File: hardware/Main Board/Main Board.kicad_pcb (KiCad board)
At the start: 4 copper layers, 65 x 56 mm, 29 parts, among them J1 Motor Power, J2 DEC Motor, J3 RA Motor, J4 Conn_01x05_Female, P1 Conn_02x20_Odd_Even, Q1 2N3904, Q2 2N3904, Q3 2N3904, Q4 2N3904, Q5 2N3904, U1 ELEGOO, U2 ELEGOO

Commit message: First Routing...
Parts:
- added J5: Joystick Connector, Connector_JST:JST_PH_B5B-PH-K_1x05_P2.00mm_Vertical, F.Cu at (253.5, 110.8)
- added J6: System Debug, Connector_PinHeader_1.27mm:PinHeader_1x03_P1.27mm_Vertical, F.Cu at (199.8, 108.2)
- added J7: DEC Debug, Connector_PinHeader_1.27mm:PinHeader_1x05_P1.27mm_Vertical, F.Cu at (206.2, 132.2)
- added J8: RA Debug, Connector_PinHeader_1.27mm:PinHeader_1x05_P1.27mm_Vertical, F.Cu at (230.0, 132.5)
- J4: value Conn_01x05_Female -> Joystick Debug; footprint Connector_JST:JST_PH_B5B-PH-K_1x05_P2.00mm_Vertical -> Connector_PinHeader_1.27mm:PinHeader_1x03_P1.27mm_Vertical
- R2, R7: value 100K -> 22K
- R5, R6: value 22K -> 100K
- U1: value ELEGOO -> RA Driver
- moved R12 38.9 mm to (246.8, 148.5), turned to 90 degrees
- moved Q5 34.7 mm to (248.8, 140.5), turned to 270 degrees
- moved R8 27.8 mm to (258.5, 130.8), turned to 90 degrees
- moved J4 27.2 mm to (259.2, 108.2), turned to 0 degrees
- moved R7 22.9 mm to (258.0, 134.8), turned to 270 degrees
- moved R11 22.5 mm to (252.0, 148.5), turned to 90 degrees
- moved R9 20.7 mm to (251.0, 136.5), turned to 90 degrees
- moved R5 19.3 mm to (242.8, 123.5), turned to 0 degrees
- moved R3 18.0 mm to (258.8, 117.6), turned to 270 degrees
- moved R4 17.8 mm to (249.7, 123.5), turned to 180 degrees
- moved R10 14.9 mm to (247.5, 134.8), turned to 270 degrees
- moved R6 14.8 mm to (254.5, 136.5), turned to 90 degrees
- moved Q3 13.9 mm to (253.5, 130.8)
- moved Q4 13.4 mm to (246.2, 130.8), turned to 90 degrees
- moved J1 10.9 mm to (219.2, 144.5)
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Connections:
- J4 pad 3: +5V -> Net-(J4-Pad3)
- P1 pad 25: Net-(P1-Pad25) -> GND
- Q1 pad 3: /GPIO10(SPI0_MOSI) -> /ID_SD
- Q2 pad 3: /ID_SD -> /GPIO22(GEN3)
- Q3 pad 3: /GPIO9(SPI0_MISO) -> /GPIO11(SPI0_SCK)
- Q4 pad 3: /GPIO25(GEN6) -> /GPIO9(SPI0_MISO)
- Q5 pad 3: /GPIO11(SPI0_SCK) -> /GPIO10(SPI0_MOSI)
- R1 pad 1: Net-(Q1-Pad2) -> +3V3
- R1 pad 2: Net-(J4-Pad5) -> /ID_SD
- R10 pad 1: Net-(Q3-Pad2) -> Net-(Q4-Pad2)
- R10 pad 2: Net-(J4-Pad1) -> Net-(J4-Pad3)
- R11 pad 1: Net-(Q4-Pad2) -> Net-(Q5-Pad2)
- R11 pad 2: Net-(J4-Pad2) -> Net-(J4-Pad1)
- R12 pad 1: Net-(Q5-Pad2) -> +3V3
- R12 pad 2: Net-(J4-Pad1) -> /GPIO10(SPI0_MOSI)
- R2 pad 1: +3V3 -> Net-(Q1-Pad2)
- R2 pad 2: /GPIO10(SPI0_MOSI) -> GND
- R3 pad 2: /ID_SD -> /GPIO22(GEN3)
- R4 pad 1: +3V3 -> Net-(Q1-Pad2)
- R4 pad 2: /GPIO9(SPI0_MISO) -> Net-(J4-Pad2)
- R5 pad 2: GND -> Net-(J4-Pad2)
- R6 pad 1: Net-(Q3-Pad2) -> +3V3
- R6 pad 2: GND -> /GPIO11(SPI0_SCK)
- R7 pad 1: +3V3 -> Net-(Q3-Pad2)
- R7 pad 2: /GPIO25(GEN6) -> GND
- R8 pad 2: /GPIO11(SPI0_SCK) -> /GPIO9(SPI0_MISO)
- R9 pad 1: Net-(Q2-Pad2) -> Net-(Q3-Pad2)
- R9 pad 2: Net-(J4-Pad2) -> Net-(J4-Pad3)
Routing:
- net /GPIO22(GEN3): track 0.00 -> 48.7 mm
- net /GPIO25(GEN6): track 43.0 -> 0.00 mm, vias 1 -> 0
- net Net-(J4-Pad3): track 0.00 -> 37.4 mm
- net /GPIO2(SDA1): track 9.48 -> 44.2 mm
- net Net-(J4-Pad1): track 28.1 -> 56.3 mm
- net /GPIO5: track 7.36 -> 34.5 mm
- net +3V3: track 0.00 -> 24.4 mm
- net /GPIO6: track 11.2 -> 35.1 mm
- net /GPIO4(GCLK): track 21.7 -> 43.2 mm
- net /GPIO3(SCL1): track 13.1 -> 34.5 mm
- net /GPIO13(PWM1): track 14.7 -> 35.6 mm
- net Net-(J4-Pad5): track 19.3 -> 0.00 mm
- net /GPIO11(SPI0_SCK): track 27.5 -> 43.9 mm
- net /ID_SD: track 14.2 -> 28.4 mm
- net /GPIO17(GEN0): track 26.4 -> 40.2 mm
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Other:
- net class Motor Power added: clearance 0.2, trace_width 0.2, via_dia 0.9, via_drill 0.6
- board text removed: "RASPBERRY-PI 40-PIN ADDON BOARD VIEW FROM TOP NOTE: P1 SHOULD BE FITTED ON THE REVERSE OF THE BOARD ADD EDGE CUTS FROM CAMERA AND DISPLAY PORTS AS REQUIRED"
- board text removed: "RJ45"
- board text removed: "USB"

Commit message: Ready to Build the Board
release_1.0
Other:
- board text added: "+"
- board text added: "-"
- board text added: "DBG"
- board text added: "DEC Motor"
- board text added: "Joystick"
- board text added: "Motor Power"
- board text added: "RA Motor"
- board text added: "https://github.com/eruditelite/pimount.git"
- board text added: "release_1.0"

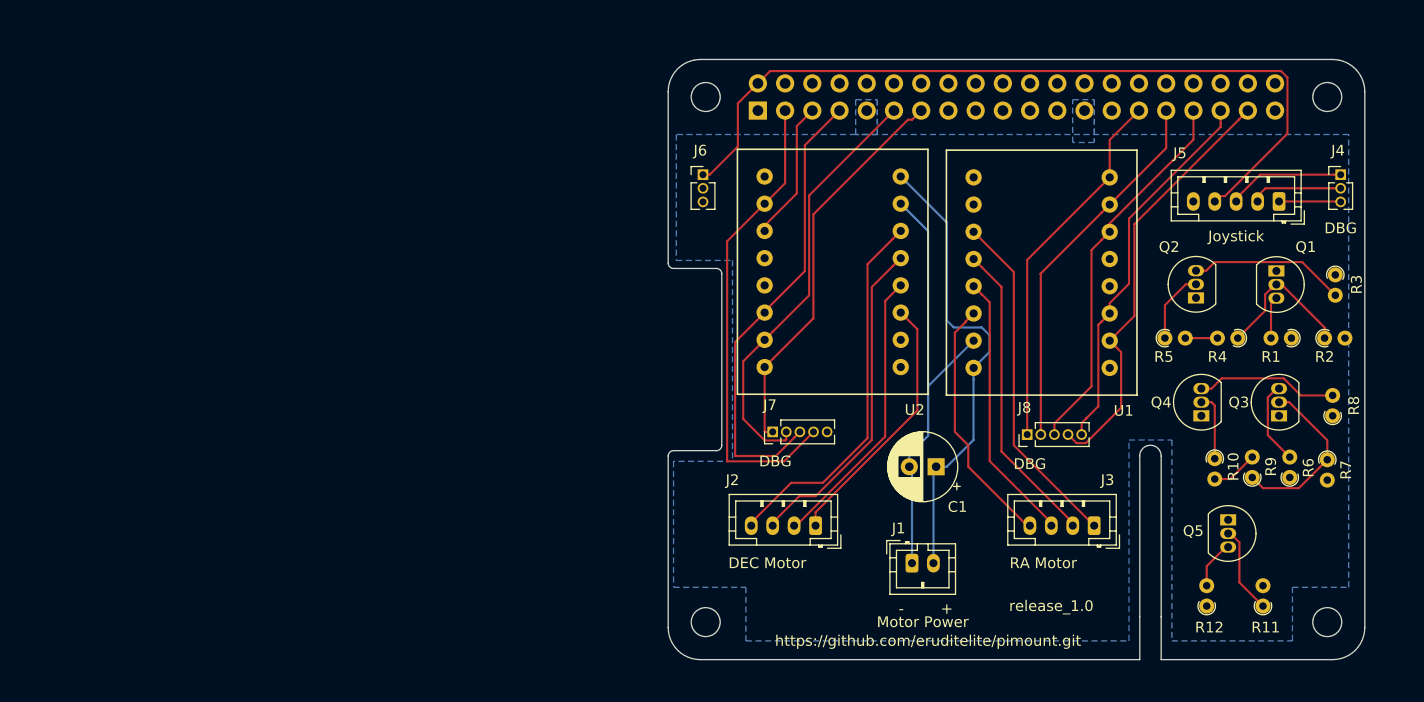
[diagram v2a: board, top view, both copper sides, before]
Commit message: Extended the Size of the Board
Include space for the DC to DC converters and
re-route.
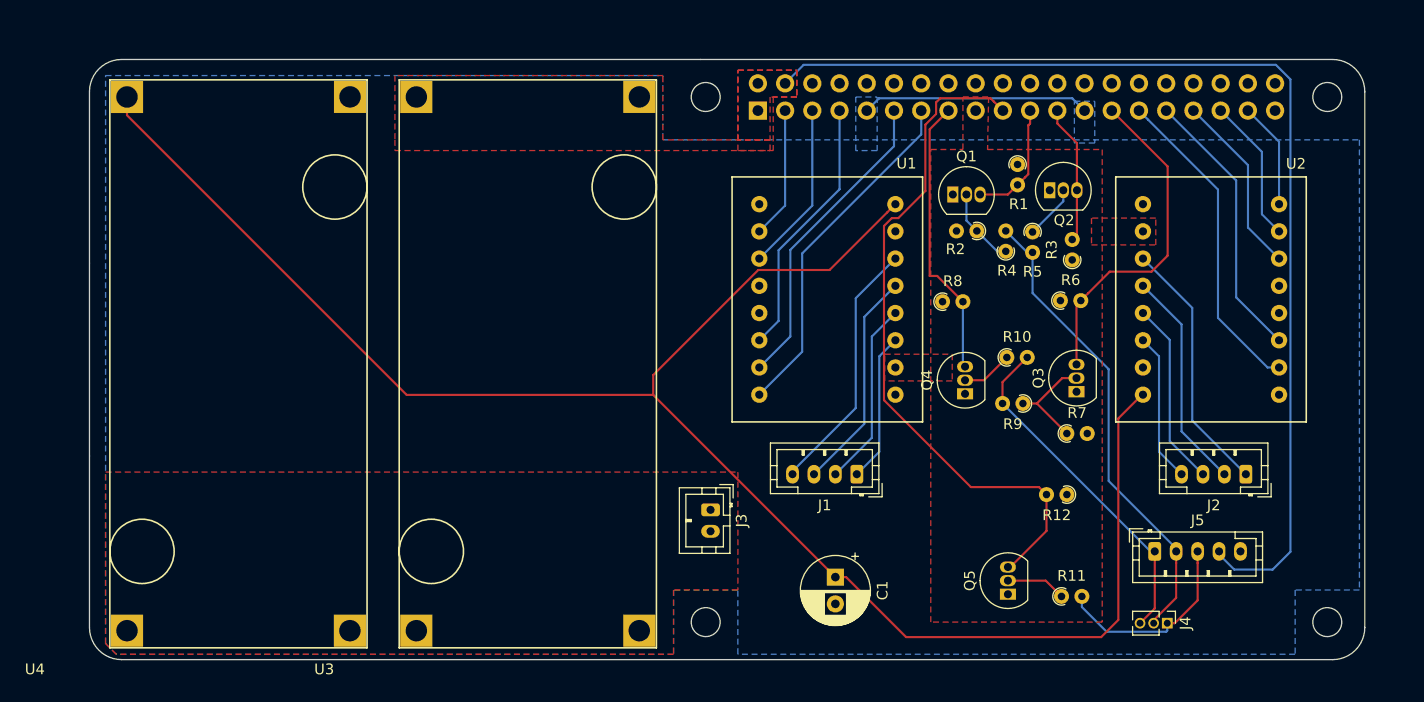
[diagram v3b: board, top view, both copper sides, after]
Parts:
- removed J6: System Debug, Connector_PinHeader_1.27mm:PinHeader_1x03_P1.27mm_Vertical
- removed J7: DEC Debug, Connector_PinHeader_1.27mm:PinHeader_1x05_P1.27mm_Vertical
- removed J8: RA Debug, Connector_PinHeader_1.27mm:PinHeader_1x05_P1.27mm_Vertical
- added U3: BuckConverter, pimount:BuckConverter, F.Cu at (171.4, 152.4)
- added U4: BuckConverter, pimount:BuckConverter, F.Cu at (144.4, 152.4)
- J1: value Motor Power -> DEC Motor; footprint Connector_JST:JST_PH_B2B-PH-K_1x02_P2.00mm_Vertical -> Connector_JST:JST_PH_B4B-PH-K_1x04_P2.00mm_Vertical
- J2: value DEC Motor -> RA Motor
- J3: value RA Motor -> Battery; footprint Connector_JST:JST_PH_B4B-PH-K_1x04_P2.00mm_Vertical -> Connector_JST:JST_PH_B2B-PH-K_1x02_P2.00mm_Vertical
- U1: value RA Driver -> ELEGOO
- U2: value ELEGOO -> RA Driver
- moved U2 52.1 mm to (253.5, 128.8), turned to 180 degrees
- moved J4 44.9 mm to (243.1, 150.1), turned to 270 degrees
- moved J2 40.4 mm to (250.4, 136.2)
- moved R8 37.9 mm to (222.1, 120.1), turned to 0 degrees
- moved U1 36.1 mm to (205.0, 111.0), turned to 0 degrees
- moved J3 35.8 mm to (200.4, 139.5), turned to 270 degrees
- moved J5 34.6 mm to (241.9, 143.4), turned to 0 degrees
- moved R2 34.0 mm to (225.3, 113.5), turned to 180 degrees
- moved Q1 31.0 mm to (223.1, 110.1), turned to 0 degrees
- moved R1 30.3 mm to (229.1, 107.3), turned to 270 degrees
- moved R6 27.0 mm to (233.1, 120.0), turned to 0 degrees
- moved R3 24.6 mm to (234.2, 116.2), turned to 90 degrees
- moved R7 24.4 mm to (233.7, 132.4), turned to 0 degrees
- moved R4 23.1 mm to (228.0, 115.4), turned to 90 degrees
- moved R9 22.5 mm to (229.6, 129.6), turned to 180 degrees
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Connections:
- C1 pad 1: Net-(C1-Pad1) -> +6V
- C1 pad 2: Net-(C1-Pad2) -> GND
- J1 pad 1: Net-(C1-Pad2) -> Net-(J1-Pad1)
- J1 pad 2: Net-(C1-Pad1) -> Net-(J1-Pad2)
- J3 pad 2: Net-(J3-Pad2) -> GND
- P1 pad 4: Net-(P1-Pad4) -> +5V
- Q1 pad 3: /ID_SD -> /GPIO9(SPI0_MISO)
- Q2 pad 3: /GPIO22(GEN3) -> /GPIO11(SPI0_SCK)
- Q3 pad 3: /GPIO11(SPI0_SCK) -> /ID_SD
- Q4 pad 3: /GPIO9(SPI0_MISO) -> /GPIO22(GEN3)
- R1 pad 2: /ID_SD -> /GPIO9(SPI0_MISO)
- R3 pad 2: /GPIO22(GEN3) -> /GPIO11(SPI0_SCK)
- R6 pad 2: /GPIO11(SPI0_SCK) -> /ID_SD
- R8 pad 2: /GPIO9(SPI0_MISO) -> /GPIO22(GEN3)
- U1 pad 11: Net-(J3-Pad1) -> Net-(J1-Pad1)
- U1 pad 12: Net-(J3-Pad2) -> Net-(J1-Pad2)
- U1 pad 13: Net-(J3-Pad3) -> Net-(J1-Pad3)
- U1 pad 14: Net-(J3-Pad4) -> Net-(J1-Pad4)
- U1 pad 15: Net-(C1-Pad2) -> GND
- U1 pad 16: Net-(C1-Pad1) -> +6V
- U1 pad 2: /GPIO26 -> /GPIO2(SDA1)
- U1 pad 3: /GPIO19(SPI1_MISO) -> /GPIO3(SCL1)
- U1 pad 6: /GPIO13(PWM1) -> /GPIO4(GCLK)
- U1 pad 7: /GPIO6 -> /GPIO17(GEN0)
- U1 pad 8: /GPIO5 -> /GPIO27(GEN2)
- U2 pad 15: Net-(C1-Pad2) -> GND
- U2 pad 16: Net-(C1-Pad1) -> +6V
- U2 pad 2: /GPIO2(SDA1) -> /GPIO5
- U2 pad 3: /GPIO3(SCL1) -> /GPIO6
- U2 pad 6: /GPIO4(GCLK) -> /GPIO13(PWM1)
- U2 pad 7: /GPIO17(GEN0) -> /GPIO19(SPI1_MISO)
- U2 pad 8: /GPIO27(GEN2) -> /GPIO26
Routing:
- net +6V: track 0.00 -> 168.1 mm
- net Net-(C1-Pad2): track 46.1 -> 0.00 mm
- net Net-(C1-Pad1): track 43.8 -> 0.00 mm
- net /GPIO9(SPI0_MISO): track 50.7 -> 11.3 mm
- net Net-(J4-Pad1): track 56.3 -> 18.9 mm
- net Net-(J3-Pad1): track 32.1 -> 0.00 mm
- net /GPIO2(SDA1): track 44.2 -> 12.3 mm
- net /GPIO11(SPI0_SCK): track 43.9 -> 13.0 mm
- net /GPIO26: track 40.2 -> 9.94 mm
- net Net-(J3-Pad2): track 28.7 -> 0.00 mm
- net Net-(J3-Pad3): track 25.3 -> 0.00 mm
- net +5V: track 75.8 -> 100.7 mm
- net +3V3: track 24.4 -> 0.00 mm
- net Net-(J1-Pad4): track 0.00 -> 24.1 mm
- net Net-(J3-Pad4): track 23.6 -> 0.00 mm
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- added copper zone on F.Cu, net +3V3
- added copper zone on F.Cu, net +5V
- added copper zone on F.Cu, net Net-(J3-Pad1)
- removed copper zone on In1.Cu, net +3V3
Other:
- board size 65 x 56 mm -> 119 x 56 mm
- board text removed: "+"
- board text removed: "-"
- board text removed: "CAMERA"
- board text removed: "DBG"
- board text removed: "DEC Motor"
- board text removed: "DISPLAY"
- board text removed: "Joystick"
- board text removed: "Motor Power"
- board text removed: "RA Motor"
- board text removed: "https://github.com/eruditelite/pimount.git"
- board text removed: "release_1.0"

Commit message: Tag and Label as Release 1.1
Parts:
- moved J4 9.96 mm to (253.0, 150.9)
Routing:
- net Net-(J4-Pad1): track 18.9 -> 31.4 mm
- net Net-(J4-Pad3): track 32.4 -> 36.8 mm
- net Net-(J4-Pad2): track 44.3 -> 47.9 mm
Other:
- copper layers 4 -> 2
- board text added: "+"
- board text added: "-"
- board text added: "Battery"
- board text added: "DEC Motor"
- board text added: "Joystick"
- board text added: "RA Motor"
- board text added: "https://github.com/eruditelite/pimount"
- board text added: "pimount release_1.1"

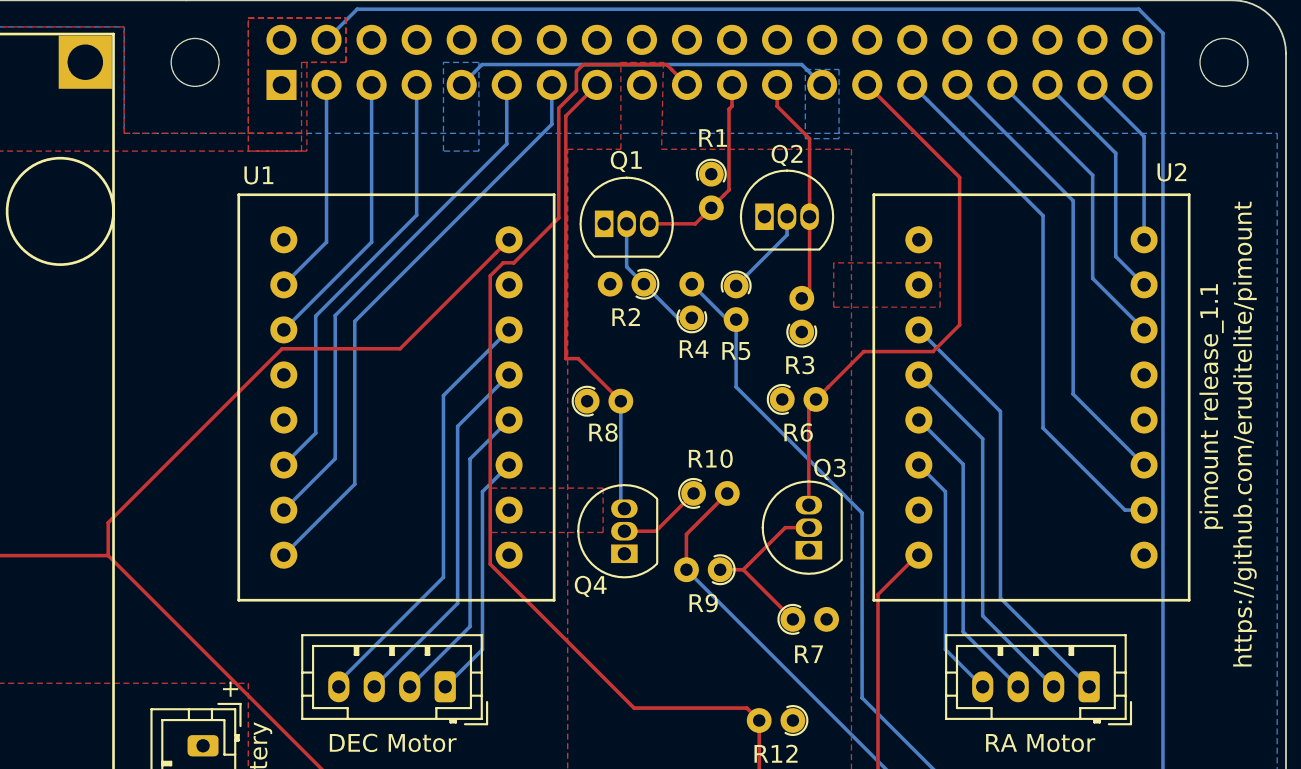
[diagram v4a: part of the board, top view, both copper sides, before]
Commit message: Update the ELEGOO Stepper Motor Footprint
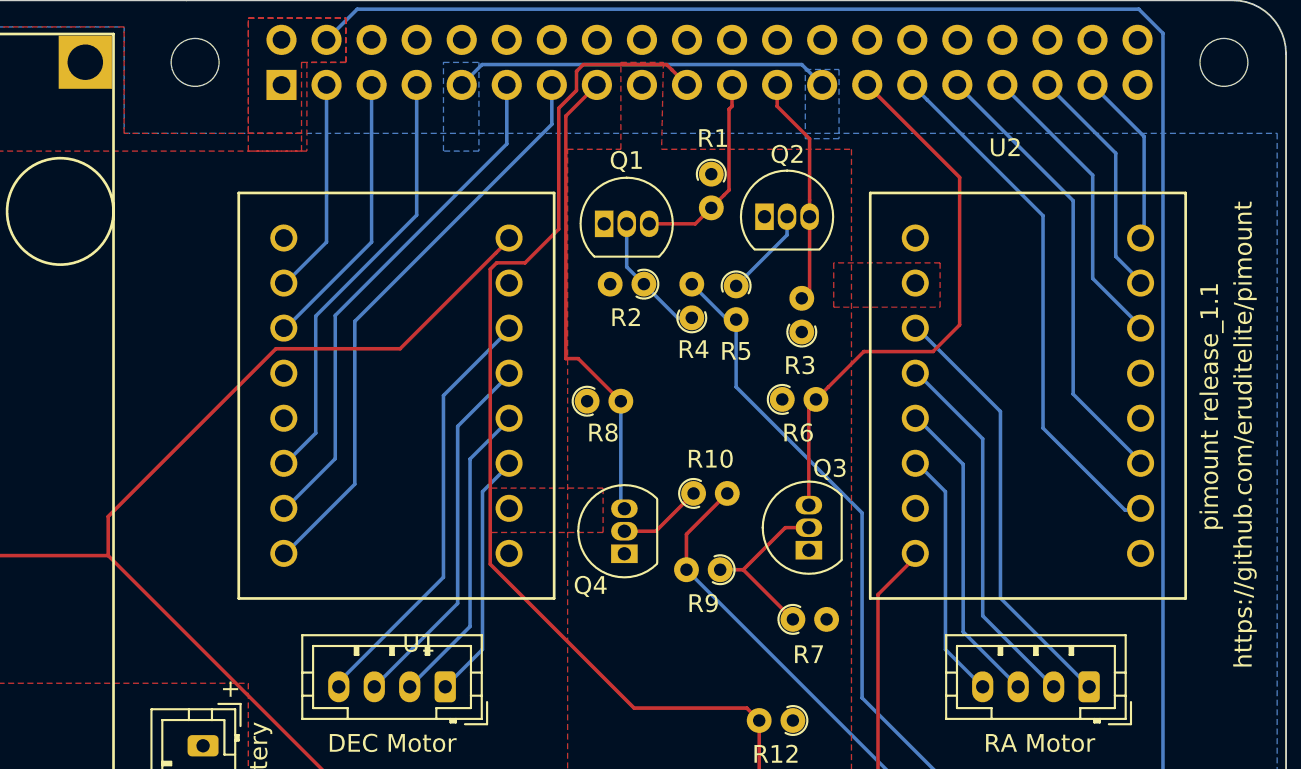
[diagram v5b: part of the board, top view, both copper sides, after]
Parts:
- moved U2 0.22 mm to (253.3, 128.7)
- moved U1 0.10 mm to (205.0, 110.9)
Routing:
- net /GPIO10(SPI0_MOSI): track 64.2 -> 64.8 mm

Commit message: Update the Circuit
Move the input on BCM 0 to BCM 12 since BCM 0 and BCM 1
are "special" (the "hat" standard requires and prom there).
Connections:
- U1 pad 5: Net-(U1-Pad5) -> /GPIO4(GCLK)
- U2 pad 5: Net-(U2-Pad5) -> /GPIO13(PWM1)
